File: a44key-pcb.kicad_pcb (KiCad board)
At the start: 2 copper layers, 132.6 x 118.3 mm, 61 parts, among them J1 AudioJack3, SW1 SW_Push, U1 ATmega32U4-AU, Y1 16MHz

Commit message: Submodules added
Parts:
- R1, R2: moved to F.Cu
- moved SW1 47.4 mm to (80.2, 96.3), turned to 90 degrees
- moved C5 33.0 mm to (92.0, 113.6), turned to 180 degrees
- moved C2 25.9 mm to (86.6, 102.7)
- moved C3 20.3 mm to (81.4, 102.7)
- moved Y1 19.2 mm to (83.6, 107.6)
- moved C6 13.5 mm to (76.6, 121.0), turned to 270 degrees
- moved R4 9.70 mm to (90.7, 131.2), turned to 0 degrees
- moved R3 9.47 mm to (77.4, 113.3)
- moved C4 8.71 mm to (76.6, 116.8), turned to 90 degrees
- moved C1 7.94 mm to (81.0, 131.4), turned to 0 degrees
- moved J1 7.64 mm to (83.8, 55.1)
- moved R2 5.49 mm to (80.2, 85.8), turned to 0 degrees
- moved R1 3.95 mm to (80.3, 88.7), turned to 0 degrees
- moved C7 1.87 mm to (81.1, 113.4), turned to 0 degrees
- moved F1 1.45 mm to (81.2, 66.5), turned to 0 degrees
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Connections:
- U1 pad 24: Net-(U1-Pad24) -> +5V
- U1 pad 44: Net-(U1-Pad24) -> +5V
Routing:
- net GND: track 187.4 -> 124.0 mm, vias 3 -> 2
- net +5V: track 94.2 -> 139.6 mm, vias 1 -> 4
- net COL5: track 69.5 -> 104.7 mm
- net Net-(R3-Pad2): track 55.0 -> 24.7 mm
- net Net-(R2-Pad1): track 25.6 -> 43.5 mm, vias 2 -> 1
- net Net-(C3-Pad1): track 9.30 -> 21.8 mm
- net Net-(R1-Pad1): track 28.8 -> 41.2 mm, vias 2 -> 1
- net Net-(C2-Pad1): track 26.7 -> 16.4 mm
- net Net-(R4-Pad2): track 2.94 -> 6.90 mm
- net Net-(D4-Pad2): track 10.3 -> 7.14 mm
- net D-: track 19.7 -> 22.7 mm, vias 1 -> 0
- net VCC: track 14.2 -> 11.7 mm
- net Net-(C6-Pad1): track 5.26 -> 4.00 mm
- net D+: track 18.8 -> 19.8 mm, vias 1 -> 0
- net (no net): track 0.00 -> 0.51 mm
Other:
- board outline removed

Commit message: Somewhat ready
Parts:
- moved F1 1.37 mm to (80.6, 65.3)
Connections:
- C1 pad 1: +5V -> VCC
- C4 pad 1: +5V -> VCC
- C5 pad 1: +5V -> VCC
- C7 pad 1: +5V -> VCC
- F1 pad 1: +5V -> VCC
- J1 pad R: R -> SCL
- J1 pad S: S -> GND
- J1 pad T: T -> VCC
- R3 pad 1: +5V -> VCC
- U1 pad 14: +5V -> VCC
- U1 pad 18: Net-(U1-Pad18) -> SCL
- U1 pad 2: +5V -> VCC
- U1 pad 24: +5V -> VCC
- U1 pad 34: +5V -> VCC
- U1 pad 44: +5V -> VCC
- U1 pad 7: +5V -> VCC
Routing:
- net VCC: track 11.7 -> 166.4 mm, vias 0 -> 4
- net +5V: track 139.6 -> 0.00 mm, vias 4 -> 0
- net SCL: track 0.00 -> 68.2 mm, vias 0 -> 1
- net GND: track 124.0 -> 156.1 mm
- added copper zone on B.Cu, net GND
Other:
- board outline added: 128.3 x 105.4 mm

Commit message: Gerbers created
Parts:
- moved J1 5.08 mm to (78.7, 55.1)
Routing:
- net SCL: track 68.2 -> 66.4 mm
- net VCC: track 166.4 -> 164.7 mm
- net GND: track 156.1 -> 154.5 mm
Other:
- board size 128.3 x 105.4 mm -> 125.4 x 104 mm

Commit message: Rewired
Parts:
- R1, R2: moved to B.Cu
- moved F1 63.0 mm to (96.8, 126.2)
- moved SW1 50.9 mm to (114.3, 58.4), turned to 180 degrees
- moved USB1 49.8 mm to (85.7, 125.4)
- moved D20 47.0 mm to (138.1, 71.4)
- moved D22 46.3 mm to (138.1, 108.7)
- moved D21 46.3 mm to (138.1, 89.8)
- moved C3 44.8 mm to (122.4, 121.0), turned to 180 degrees
- moved C2 44.6 mm to (122.1, 129.7), turned to 0 degrees
- moved Y1 42.7 mm to (122.4, 125.4), turned to 0 degrees
- moved D17 39.9 mm to (141.3, 71.4)
- moved R3 39.4 mm to (116.6, 117.7), turned to 270 degrees
- moved D19 39.3 mm to (141.3, 108.7)
- moved D18 39.3 mm to (141.3, 89.7)
- moved C4 36.5 mm to (113.1, 116.9), turned to 0 degrees
- moved C7 36.3 mm to (116.5, 121.4), turned to 270 degrees
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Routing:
- net ROW0: track 92.6 -> 15.9 mm
- net ROW1: track 92.4 -> 16.0 mm
- net ROW2: track 91.8 -> 16.0 mm
- net GND: track 154.5 -> 215.1 mm, vias 2 -> 4
- net Net-(R3-Pad2): track 24.7 -> 75.2 mm
- net Net-(D22-Pad2): track 18.5 -> 61.9 mm
- net Net-(D4-Pad2): track 7.14 -> 47.9 mm
- net SCL: track 66.4 -> 104.0 mm
- net Net-(R1-Pad1): track 41.2 -> 5.33 mm, vias 1 -> 0
- net COL4: track 65.0 -> 100.1 mm
- net Net-(R2-Pad1): track 43.5 -> 8.66 mm, vias 1 -> 0
- net Net-(D21-Pad2): track 29.0 -> 63.0 mm
- net Net-(D20-Pad2): track 27.3 -> 61.1 mm
- net ROW3: track 39.8 -> 9.58 mm
- net Net-(D8-Pad2): track 7.15 -> 35.1 mm
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- removed copper zone on B.Cu, net GND

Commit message: Rewired
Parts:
- F1: moved to B.Cu
- J1: footprint Connector_Audio:Jack_3.5mm_CUI_SJ1-3535NG_Horizontal -> SJ-43514:CUI_SJ-43514
- MX1, MX10, MX11, MX12, MX13, MX14, MX15, MX16, MX17, MX18, MX19, MX2, MX20, MX21, MX22, MX3, MX4, MX5, MX6, MX7, MX8, MX9: footprint MX_Alps_Hybrid:MX-1U-NoLED -> MX_Alps_Hybrid:MX-Alps-Choc-X-1U-NoLED
- moved USB1 104.4 mm to (159.5, 51.6), turned to 180 degrees
- moved F1 86.4 mm to (148.8, 57.1)
- moved R2 77.6 mm to (148.6, 50.8), turned to 0 degrees
- moved R1 77.5 mm to (148.6, 53.2), turned to 0 degrees
- moved C5 72.6 mm to (101.0, 63.1), turned to 315 degrees
- moved Y1 71.8 mm to (121.7, 53.5)
- moved C2 71.3 mm to (123.2, 58.4), turned to 315 degrees
- moved R3 68.9 mm to (121.4, 49.0), turned to 0 degrees
- moved C3 67.9 mm to (128.3, 53.3), turned to 315 degrees
- moved C7 66.9 mm to (100.1, 56.5), turned to 135 degrees
- moved U1 66.7 mm to (110.8, 59.1), turned to 315 degrees
- moved C4 66.6 mm to (115.7, 50.4), turned to 45 degrees
- moved C6 64.9 mm to (104.5, 52.2), turned to 135 degrees
- moved R4 64.6 mm to (108.4, 69.5), turned to 45 degrees
- moved C1 52.9 mm to (105.5, 68.8), turned to 225 degrees
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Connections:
- U1 pad 1: Net-(U1-Pad1) -> ROW1
- U1 pad 10: Net-(U1-Pad10) -> COL4
- U1 pad 11: Net-(U1-Pad11) -> COL3
- U1 pad 27: Net-(U1-Pad27) -> ROW0
- U1 pad 28: Net-(U1-Pad28) -> ROW2
- U1 pad 29: Net-(U1-Pad29) -> ROW3
- U1 pad 30: Net-(U1-Pad30) -> COL5
- U1 pad 36: Net-(U1-Pad36) -> COL1
- U1 pad 37: Net-(U1-Pad37) -> COL0
- U1 pad 9: Net-(U1-Pad9) -> COL2
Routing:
- net COL0: track 38.7 -> 232.4 mm, vias 0 -> 2
- net COL1: track 38.1 -> 202.8 mm, vias 0 -> 2
- net COL2: track 57.2 -> 198.3 mm, vias 0 -> 1
- net COL3: track 57.2 -> 191.2 mm, vias 0 -> 1
- net COL5: track 90.7 -> 205.5 mm, vias 1 -> 3
- net ROW3: track 9.58 -> 93.2 mm, vias 0 -> 2
- net ROW1: track 16.0 -> 94.9 mm, vias 0 -> 2
- net COL4: track 100.1 -> 176.8 mm, vias 0 -> 2
- net SCL: track 104.0 -> 31.7 mm, vias 1 -> 2
- net GND: track 215.1 -> 145.9 mm, vias 4 -> 8
- net ROW2: track 16.0 -> 74.5 mm, vias 0 -> 3
- net Net-(R1-Pad1): track 5.33 -> 53.5 mm, vias 0 -> 2
- net Net-(R2-Pad1): track 8.66 -> 54.3 mm, vias 0 -> 2
- net Net-(D5-Pad2): track 8.94 -> 49.1 mm
- net Net-(R3-Pad2): track 75.2 -> 44.8 mm, vias 1 -> 3
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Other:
- board size 125.4 x 104 mm -> 125.4 x 107.2 mm

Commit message: Rewired
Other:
- board size 125.4 x 107.2 mm -> 116.6 x 105.5 mm

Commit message: Covered with zones
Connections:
- C1 pad 1: VCC -> +5V
- C4 pad 1: VCC -> +5V
- C5 pad 1: VCC -> +5V
- C7 pad 1: VCC -> +5V
- F1 pad 1: VCC -> +5V
- J1 pad 2: VCC -> +5V
- R3 pad 1: VCC -> +5V
- U1 pad 14: VCC -> +5V
- U1 pad 2: VCC -> +5V
- U1 pad 24: VCC -> +5V
- U1 pad 34: VCC -> +5V
- U1 pad 44: VCC -> +5V
- U1 pad 7: VCC -> +5V
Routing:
- net VCC: track 161.8 -> 7.93 mm, vias 6 -> 1
- net +5V: track 0.00 -> 153.9 mm, vias 0 -> 5
- net Net-(USB1-Pad6): track 0.00 -> 16.3 mm
- net Net-(C2-Pad1): track 10.7 -> 11.7 mm
- added copper zone on B.Cu, net GND
- added copper zone on F.Cu, net GND

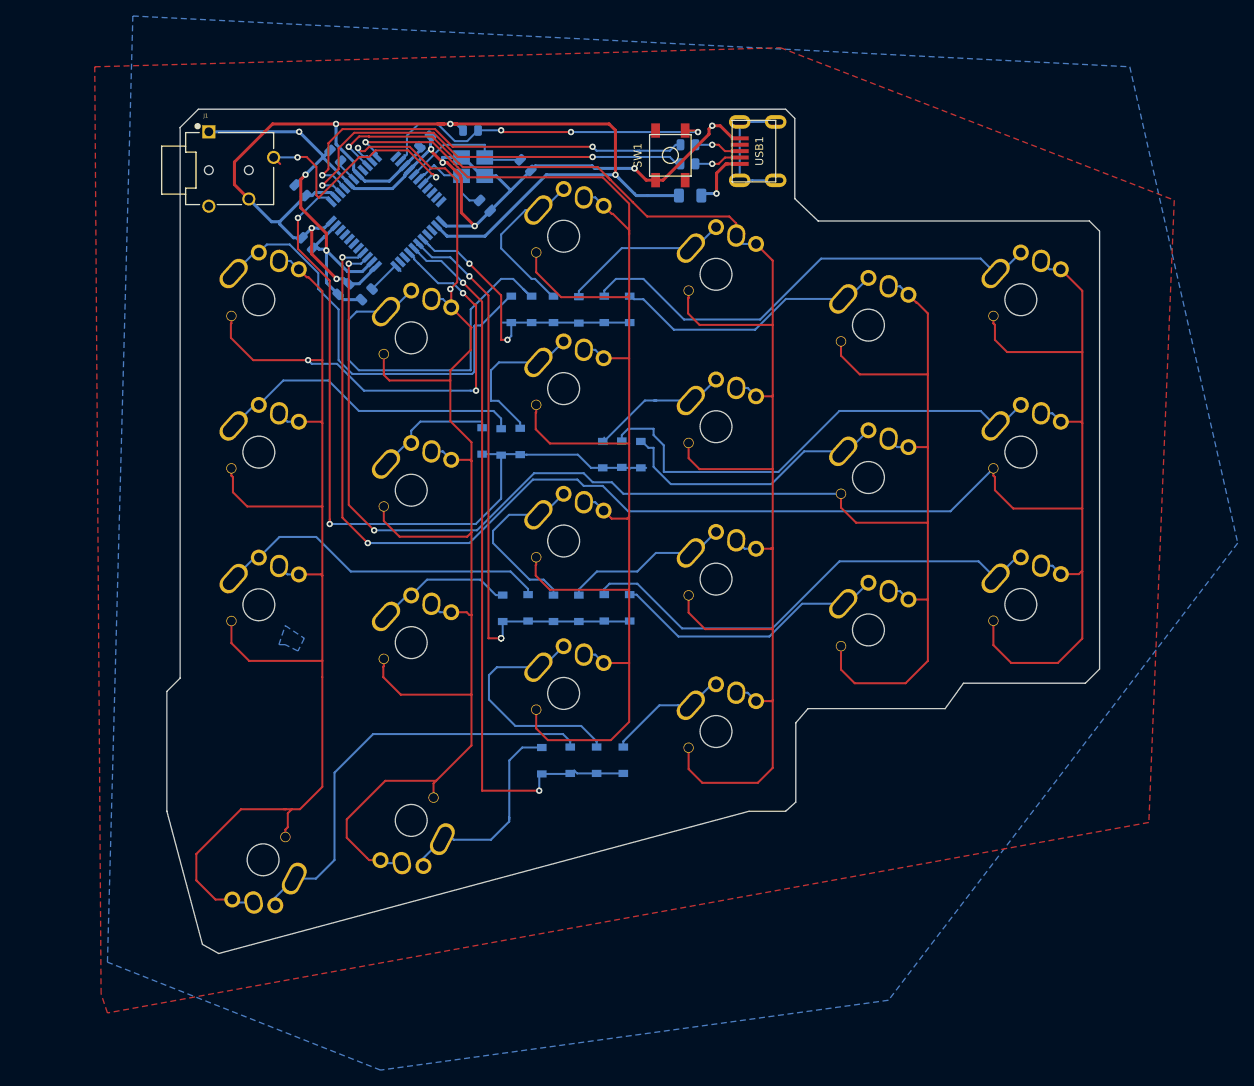
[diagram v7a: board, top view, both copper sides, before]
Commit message: Added raisers for the thumbs
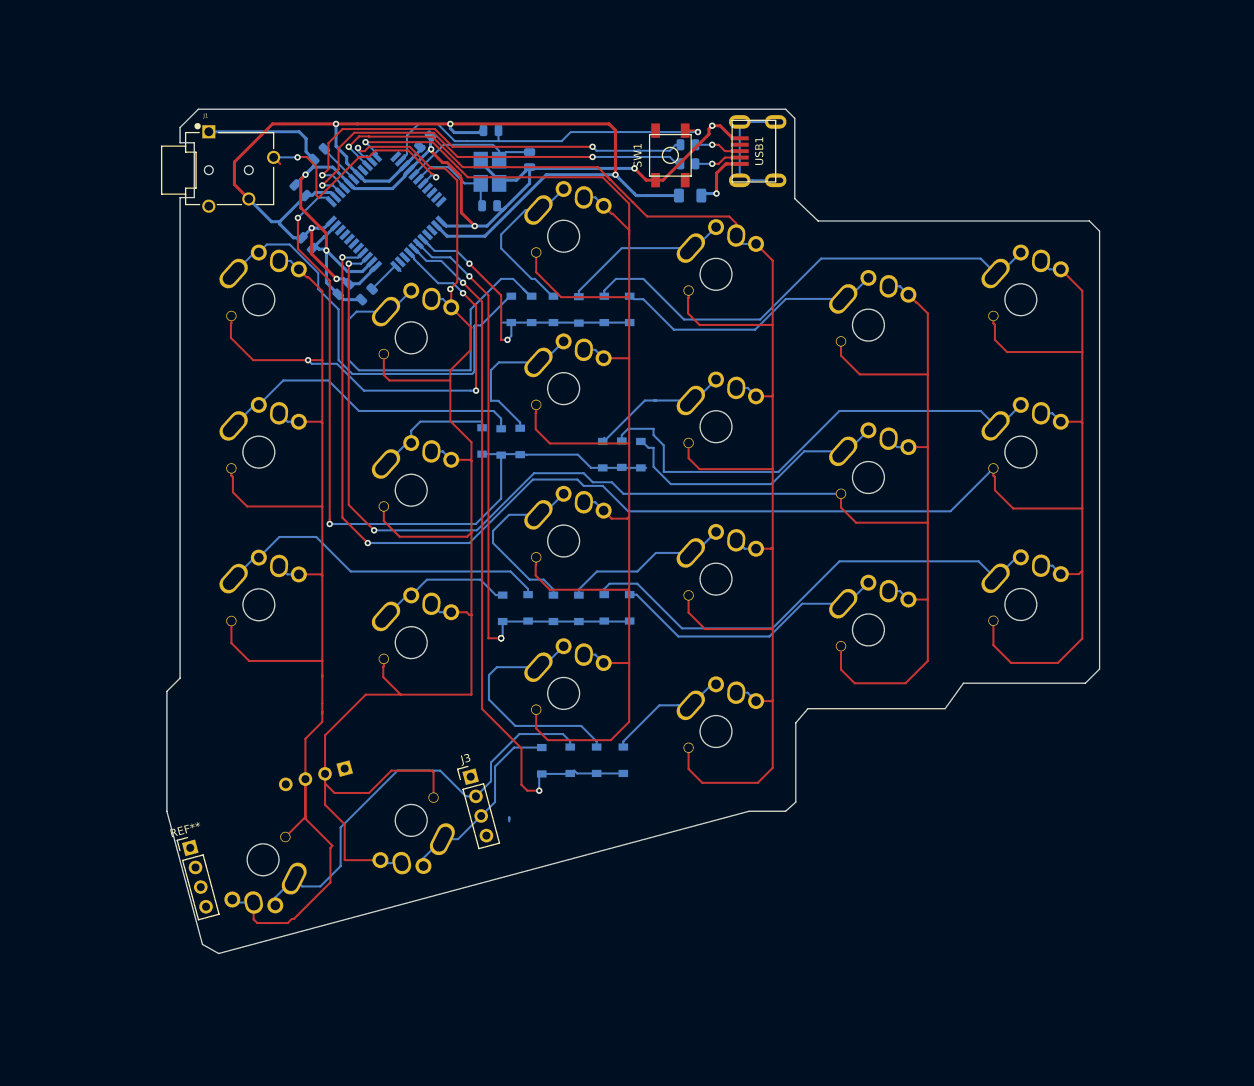
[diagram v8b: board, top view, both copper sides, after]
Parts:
- added J2: Conn_01x04_Female, Connector_PinHeader_2.54mm:PinHeader_1x04_P2.54mm_Vertical, B.Cu at (105.7, 128.8)
- added J3: Conn_01x04_Female, Connector_PinHeader_2.54mm:PinHeader_1x04_P2.54mm_Vertical, F.Cu at (121.4, 129.8)
- added REF**: PinHeader_1x04_P2.54mm_Vertical, Connector_PinHeader_2.54mm:PinHeader_1x04_P2.54mm_Vertical, F.Cu at (86.4, 138.7)
- moved R3 2.56 mm to (124.0, 49.0)
- moved Y1 2.20 mm to (123.8, 54.2), turned to 90 degrees
- moved C6 2.04 mm to (102.5, 52.0), turned to 225 degrees
- moved C3 0.85 mm to (128.8, 52.7), turned to 270 degrees
- moved C2 0.59 mm to (123.8, 58.4), turned to 0 degrees
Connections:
- net Net-(D4-Pad2) renamed TH35
- net Net-(D8-Pad2) renamed TH34
- Y1 pad 1: GND -> Net-(C2-Pad1)
- Y1 pad 2: Net-(C3-Pad1) -> GND
- Y1 pad 3: GND -> Net-(C3-Pad1)
- Y1 pad 4: Net-(C2-Pad1) -> GND
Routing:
- net COL4: track 176.8 -> 193.5 mm
- net COL5: track 205.5 -> 210.5 mm
- net ROW3: track 93.2 -> 89.9 mm
- net Net-(C6-Pad1): track 2.84 -> 5.48 mm
- net TH34: track 26.3 -> 24.1 mm
- net GND: track 146.1 -> 144.0 mm, vias 8 -> 6
- net +5V: track 153.9 -> 155.4 mm
- net TH35: track 53.8 -> 55.1 mm
- net Net-(R3-Pad2): track 44.8 -> 45.8 mm, vias 3 -> 1
- net Net-(D8-Pad2): track 0.00 -> 0.76 mm
- net Net-(C2-Pad1): track 11.7 -> 12.2 mm
- removed copper zone on B.Cu, net GND
- removed copper zone on F.Cu, net GND
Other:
- outline, holes or cut-outs redrawn
